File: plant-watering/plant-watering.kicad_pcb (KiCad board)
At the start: 2 copper layers, 11 parts, among them J1 Conn_01x03_Male, J2 Conn_01x03_Male, J3 Conn_01x03_Male, J4 Screw_Terminal_01x02, Q1 BC337, Q2 BC337, Q3 BC337, U1 ESP32-DEVKITC-32D

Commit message: added many schematicy
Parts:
- added J5: Screw_Terminal_01x02, Terminal_Blocks:TerminalBlock_bornier-2_P5.08mm, F.Cu at (142.2, 89.4)
- added J6: Screw_Terminal_01x02, Terminal_Blocks:TerminalBlock_bornier-2_P5.08mm, F.Cu at (142.2, 98.5)
- added J7: Screw_Terminal_01x02, Terminal_Blocks:TerminalBlock_bornier-2_P5.08mm, F.Cu at (153.8, 89.4)
- added K1: HJR-4102-L-05V, HJR-4102-L-05V:RELAY_HJR-4102-L-05V, F.Cu at (148.3, 62.5)
- added K2: HJR-4102-L-05V, HJR-4102-L-05V:RELAY_HJR-4102-L-05V, F.Cu at (148.3, 74.5)
- added K3: HJR-4102-L-05V, HJR-4102-L-05V:RELAY_HJR-4102-L-05V, F.Cu at (166.2, 62.5)
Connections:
- J3 pad 3: GPIO33 -> GPIO32
- U1 pad 5: Net-(U1-Pad5) -> GPIO34
- U1 pad 7: Net-(U1-Pad7) -> GPIO32
- U1 pad 8: Net-(U1-Pad8) -> GPIO33

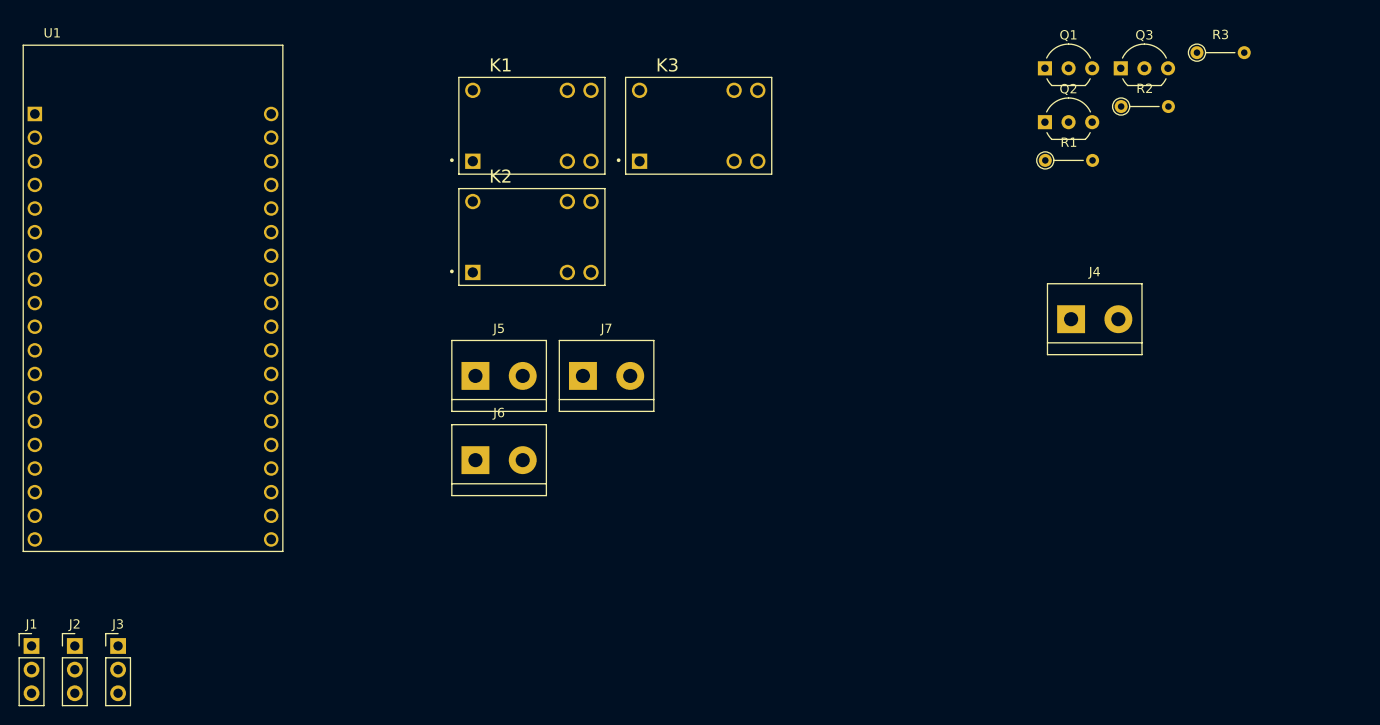
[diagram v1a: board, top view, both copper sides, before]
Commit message: edited schematic & started pcb design
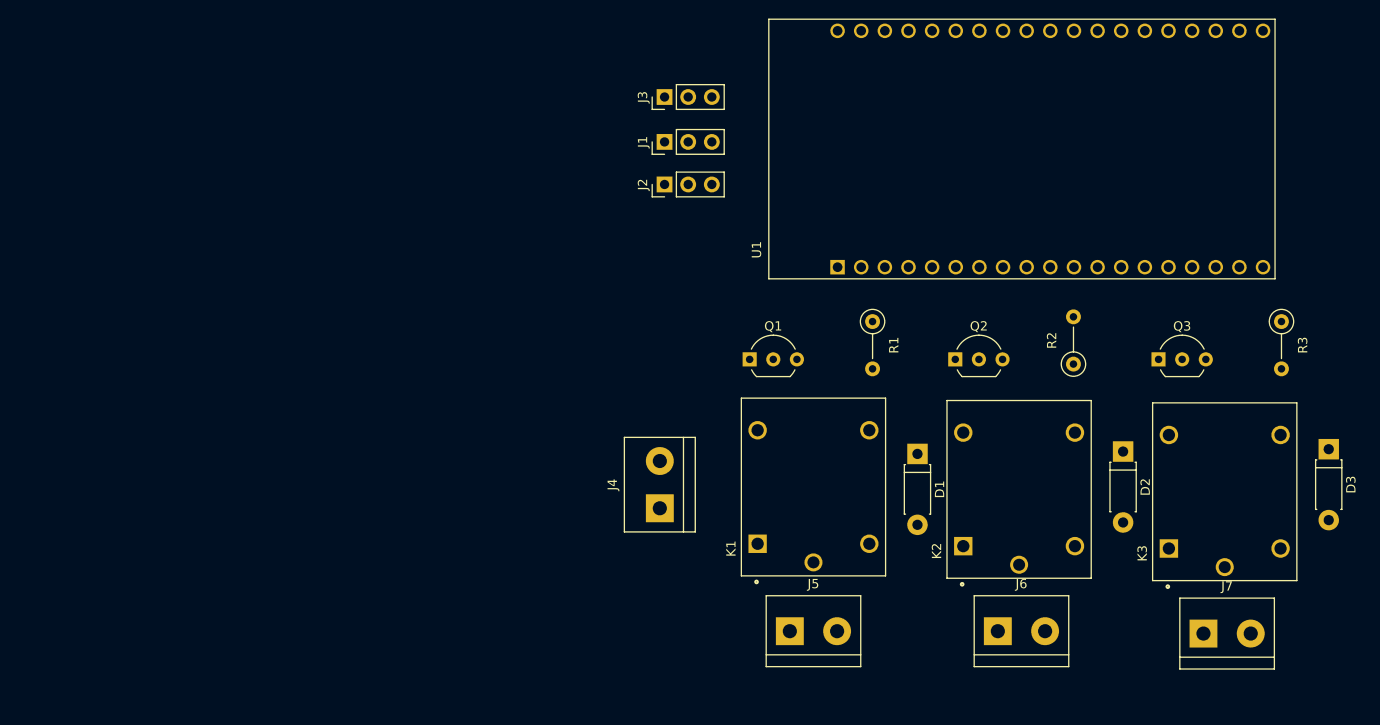
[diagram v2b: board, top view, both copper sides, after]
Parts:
- added D1: D, Diodes_ThroughHole:D_DO-41_SOD81_P7.62mm_Horizontal, F.Cu at (189.7, 97.8)
- added D2: D, Diodes_ThroughHole:D_DO-41_SOD81_P7.62mm_Horizontal, F.Cu at (211.8, 97.5)
- added D3: D, Diodes_ThroughHole:D_DO-41_SOD81_P7.62mm_Horizontal, F.Cu at (233.9, 97.3)
- J4: value Screw_Terminal_01x02 -> Input
- J5: value Screw_Terminal_01x02 -> M1
- J6: value Screw_Terminal_01x02 -> M2
- J7: value Screw_Terminal_01x02 -> M3
- K1, K2, K3: value HJR-4102-L-05V -> SRD-05VDC-SL-C; footprint HJR-4102-L-05V:RELAY_HJR-4102-L-05V -> SRD-05VDC-SL-C:RELAY_SRD-05VDC-SL-C
- R1, R2, R3: footprint Resistors:R_Axial_DIN0204_L3.6mm_D1.6mm_P5.08mm_Vertical -> Resistors_ThroughHole:R_Axial_DIN0207_L6.3mm_D2.5mm_P5.08mm_Vertical
- moved U1 94.7 mm to (200.9, 65.0), turned to 90 degrees
- moved J1 87.0 mm to (162.6, 64.3), turned to 90 degrees
- moved J3 83.2 mm to (162.6, 59.4), turned to 90 degrees
- moved J2 80.5 mm to (162.6, 68.8), turned to 90 degrees
- moved J7 72.2 mm to (220.5, 117.1)
- moved K3 68.9 mm to (222.8, 101.9), turned to 90 degrees
- moved J6 59.1 mm to (198.4, 116.8)
- moved K2 59.0 mm to (200.7, 101.6), turned to 90 degrees
- moved K1 49.2 mm to (178.6, 101.3), turned to 90 degrees
- moved J4 48.6 mm to (162.1, 103.6), turned to 90 degrees
- moved Q1 44.6 mm to (171.7, 87.6)
- moved J5 43.5 mm to (176.0, 116.8)
- moved Q3 31.5 mm to (215.6, 87.6)
- moved R3 30.3 mm to (228.9, 83.6), turned to 270 degrees
- moved R2 28.1 mm to (206.5, 88.1), turned to 90 degrees
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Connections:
- J4 pad 1: +5V -> GND
- J4 pad 2: GND -> +5V
- J5 pad 1: M1 -> GND
- J5 pad 2: GND -> M1
- J6 pad 1: M2 -> GND
- J6 pad 2: GND -> M2
- J7 pad 1: M3 -> GND
- J7 pad 2: GND -> M3
- Q1 pad 1: +5V -> RelayS1
- Q1 pad 3: RelayS1 -> GND
- Q2 pad 1: +5V -> RelayS2
- Q2 pad 3: RelayS2 -> GND
- Q3 pad 1: +5V -> RelayS3
- Q3 pad 3: RelayS3 -> GND

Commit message: started pcb design
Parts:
- added REF**: MountingHole_3.2mm_M3, MountingHole:MountingHole_3.2mm_M3, F.Cu at (234.5, 54.9)
- added REF**: MountingHole_3.2mm_M3, MountingHole:MountingHole_3.2mm_M3, F.Cu at (234.5, 116.8)
- added REF**: MountingHole_3.2mm_M3, MountingHole:MountingHole_3.2mm_M3, F.Cu at (161.5, 116.8)
- added REF**: MountingHole_3.2mm_M3, MountingHole:MountingHole_3.2mm_M3, F.Cu at (161.5, 54.9)
- moved J3 9.20 mm to (168.4, 52.3), turned to 0 degrees
- moved J2 7.12 mm to (168.4, 72.9), turned to 0 degrees
- moved J1 6.11 mm to (168.4, 62.5), turned to 0 degrees
- moved J4 5.57 mm to (164.3, 98.6), turned to 270 degrees
- moved R2 5.08 mm to (206.5, 83.1), turned to 270 degrees
- moved U1 0.51 mm to (200.9, 65.5)
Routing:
- added copper zone on B.Cu, net GND

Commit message: added several parts#
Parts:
- added D4: D, Diodes_ThroughHole:D_DO-41_SOD81_P7.62mm_Horizontal, F.Cu at (266.2, 80.8)
- added D5: D, Diodes_ThroughHole:D_DO-41_SOD81_P7.62mm_Horizontal, F.Cu at (266.2, 76.3)
- added D6: D, Diodes_ThroughHole:D_DO-41_SOD81_P7.62mm_Horizontal, F.Cu at (287.5, 59.3)
- added J10: Conn_01x03_Male, Pin_Headers:Pin_Header_Straight_1x03_Pitch2.54mm, F.Cu at (320.2, 76.9)
- added J11: M1, Terminal_Blocks:TerminalBlock_bornier-2_P5.08mm, F.Cu at (257.8, 99.7)
- added J12: M2, Terminal_Blocks:TerminalBlock_bornier-2_P5.08mm, F.Cu at (246.3, 108.8)
- added J13: M3, Terminal_Blocks:TerminalBlock_bornier-2_P5.08mm, F.Cu at (246.3, 99.7)
- added J14: Conn_01x04_Female, Pin_Headers:Pin_Header_Straight_1x04_Pitch2.54mm, F.Cu at (283.0, 97.5)
- added J8: Conn_01x03_Male, Pin_Headers:Pin_Header_Straight_1x03_Pitch2.54mm, F.Cu at (310.9, 76.9)
- added J9: Conn_01x03_Male, Pin_Headers:Pin_Header_Straight_1x03_Pitch2.54mm, F.Cu at (315.5, 76.9)
- added K4: SRD-05VDC-SL-C, SRD-05VDC-SL-C:RELAY_SRD-05VDC-SL-C, F.Cu at (275.3, 65.6)
- added K5: SRD-05VDC-SL-C, SRD-05VDC-SL-C:RELAY_SRD-05VDC-SL-C, F.Cu at (254.0, 82.6)
- added K6: SRD-05VDC-SL-C, SRD-05VDC-SL-C:RELAY_SRD-05VDC-SL-C, F.Cu at (254.0, 65.6)
- added Q4: BC337, TO_SOT_Packages_THT:TO-92_Inline_Wide, F.Cu at (327.1, 64.6)
- added Q5: BC337, TO_SOT_Packages_THT:TO-92_Inline_Wide, F.Cu at (318.9, 64.6)
- added Q6: BC337, TO_SOT_Packages_THT:TO-92_Inline_Wide, F.Cu at (310.1, 68.8)
- added R4: 5k, Resistors_ThroughHole:R_Axial_DIN0207_L6.3mm_D2.5mm_P5.08mm_Vertical, F.Cu at (319.5, 59.2)
- added R5: 5k, Resistors_ThroughHole:R_Axial_DIN0207_L6.3mm_D2.5mm_P5.08mm_Vertical, F.Cu at (310.7, 63.4)
- added R6: 5k, Resistors_ThroughHole:R_Axial_DIN0207_L6.3mm_D2.5mm_P5.08mm_Vertical, F.Cu at (310.7, 59.2)
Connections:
- R2 pad 1: GPIO14 -> GPIO13
- R3 pad 1: GPIO27 -> GPIO17
- U1 pad 12: GPIO14 -> Net-(U1-Pad12)
- U1 pad 15: Net-(U1-Pad15) -> GPIO13
- U1 pad 22: Net-(U1-Pad22) -> GPIO22
- U1 pad 25: Net-(U1-Pad25) -> GPIO21
- U1 pad 30: Net-(U1-Pad30) -> GPIO17
- U1 pad 31: Net-(U1-Pad31) -> GPIO16
- U1 pad 6: Net-(U1-Pad6) -> GPIO35

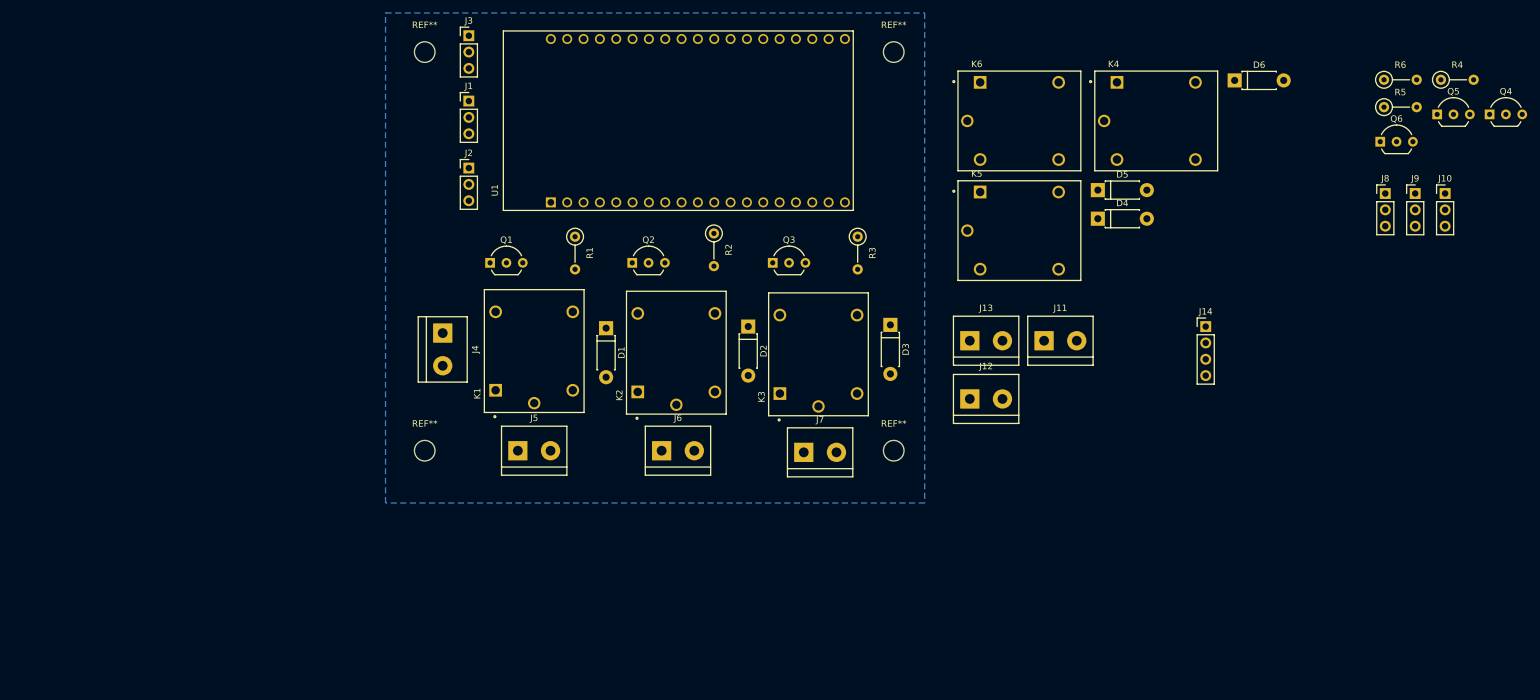
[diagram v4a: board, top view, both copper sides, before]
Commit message: changed pcb parts
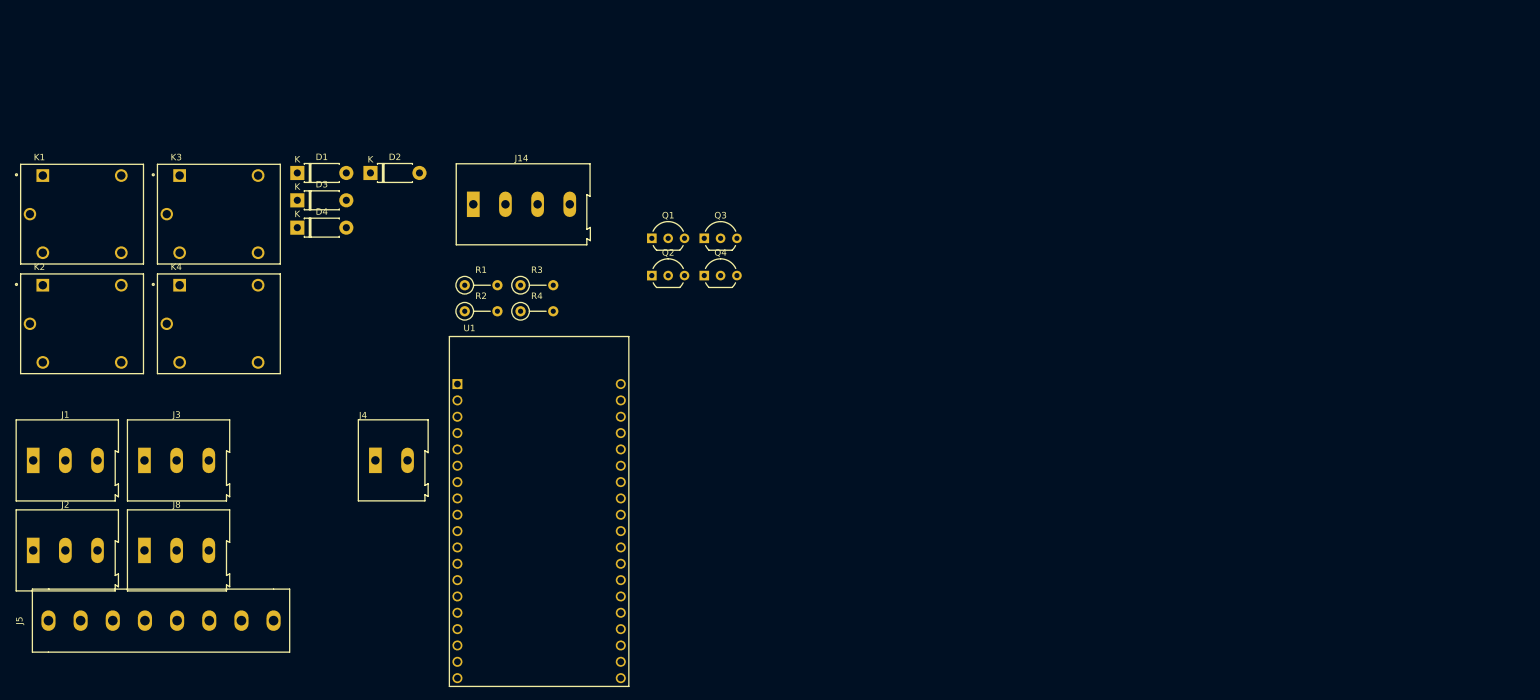
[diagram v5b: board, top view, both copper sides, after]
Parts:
- removed D5, D6: D, Diodes_ThroughHole:D_DO-41_SOD81_P7.62mm_Horizontal
- removed J10, J9: Conn_01x03_Male, Pin_Headers:Pin_Header_Straight_1x03_Pitch2.54mm
- removed J11: M1, Terminal_Blocks:TerminalBlock_bornier-2_P5.08mm
- removed J12, J6: M2, Terminal_Blocks:TerminalBlock_bornier-2_P5.08mm
- removed J13, J7: M3, Terminal_Blocks:TerminalBlock_bornier-2_P5.08mm
- removed K5, K6: SRD-05VDC-SL-C, SRD-05VDC-SL-C:RELAY_SRD-05VDC-SL-C
- removed Q5, Q6: BC337, TO_SOT_Packages_THT:TO-92_Inline_Wide
- removed R5, R6: 5k, Resistors_ThroughHole:R_Axial_DIN0207_L6.3mm_D2.5mm_P5.08mm_Vertical
- removed REF** (x4): MountingHole_3.2mm_M3, MountingHole:MountingHole_3.2mm_M3
- D1, D2, D3, D4: footprint Diodes_ThroughHole:D_DO-41_SOD81_P7.62mm_Horizontal -> Diode_THT:D_DO-41_SOD81_P7.62mm_Horizontal
- J1, J2, J3, J8: footprint Pin_Headers:Pin_Header_Straight_1x03_Pitch2.54mm -> TerminalBlock:TerminalBlock_Altech_AK300-3_P5.00mm
- J14: footprint Pin_Headers:Pin_Header_Straight_1x04_Pitch2.54mm -> TerminalBlock:TerminalBlock_Altech_AK300-4_P5.00mm
- J4: footprint Terminal_Blocks:TerminalBlock_bornier-2_P5.08mm -> TerminalBlock:TerminalBlock_Altech_AK300-2_P5.00mm
- J5: value M1 -> Screw_Terminal_01x08; footprint Terminal_Blocks:TerminalBlock_bornier-2_P5.08mm -> TerminalBlock:ScrewTerminal_1x8_P5.00
- Q1, Q2, Q3, Q4: footprint TO_SOT_Packages_THT:TO-92_Inline_Wide -> Package_TO_SOT_THT:TO-92_Inline_Wide
- R1, R2, R3, R4: footprint Resistors_ThroughHole:R_Axial_DIN0207_L6.3mm_D2.5mm_P5.08mm_Vertical -> Resistor_THT:R_Axial_DIN0207_L6.3mm_D2.5mm_P5.08mm_Vertical
- moved J8 200.7 mm to (118.0, 132.3)
- moved K4 149.1 mm to (129.5, 97.1)
- moved R4 147.5 mm to (176.4, 95.2)
- moved Q4 124.6 mm to (205.0, 89.6)
- moved D4 124.5 mm to (141.7, 82.2)
- moved J14 115.4 mm to (169.1, 78.5)
- moved K3 95.7 mm to (129.5, 80.1), turned to 0 degrees
- moved D3 94.2 mm to (141.7, 77.9), turned to 0 degrees
- moved K2 92.5 mm to (108.3, 97.1), turned to 0 degrees
- moved J2 90.1 mm to (100.7, 132.3)
- moved J1 87.8 mm to (100.7, 118.3)
- moved J3 83.1 mm to (118.0, 118.3)
- moved J5 82.3 mm to (98.0, 143.3), turned to 90 degrees
- moved K1 73.4 mm to (108.3, 80.1), turned to 0 degrees
- moved U1 64.4 mm to (179.3, 126.2), turned to 0 degrees
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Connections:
- J5 pad 1: GND -> M1
- J5 pad 2: M1 -> GND
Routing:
- removed copper zone on B.Cu, net GND

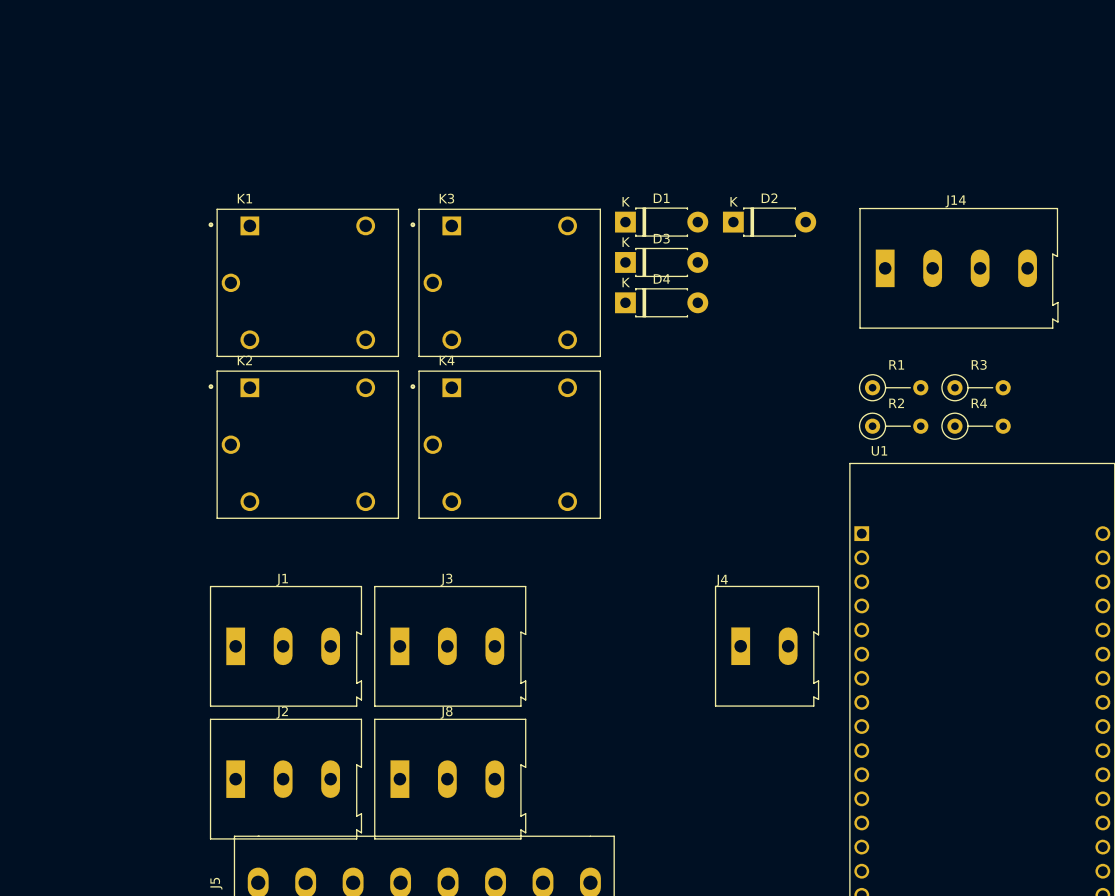
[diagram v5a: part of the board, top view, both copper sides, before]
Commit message: changed parts on pcb
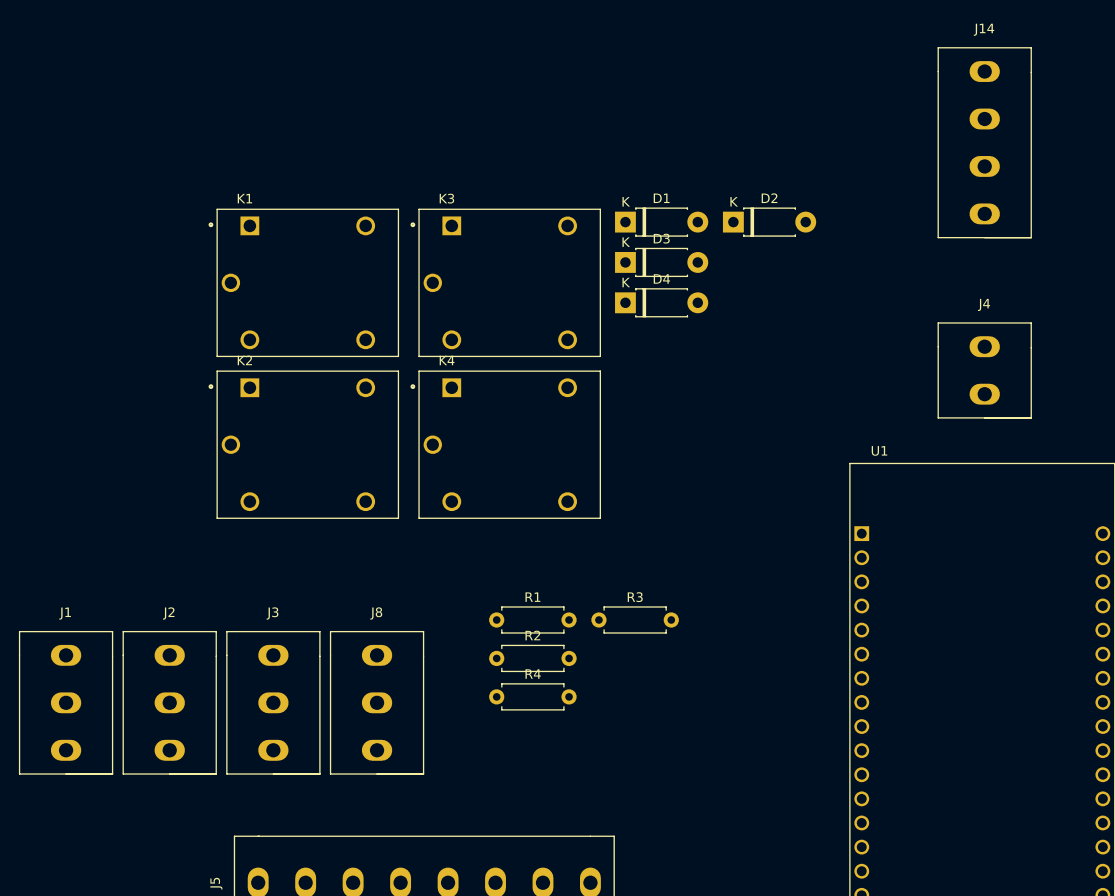
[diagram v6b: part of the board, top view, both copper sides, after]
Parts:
- J1, J2, J3, J8: footprint TerminalBlock:TerminalBlock_Altech_AK300-3_P5.00mm -> TerminalBlock:ScrewTerminal_1x3_P5.00
- J14: footprint TerminalBlock:TerminalBlock_Altech_AK300-4_P5.00mm -> TerminalBlock:ScrewTerminal_1x4_P5.00
- J4: footprint TerminalBlock:TerminalBlock_Altech_AK300-2_P5.00mm -> TerminalBlock:ScrewTerminal_1x2_P5.00
- R1, R2, R3, R4: footprint Resistor_THT:R_Axial_DIN0207_L6.3mm_D2.5mm_P5.08mm_Vertical -> Resistor_THT:R_Axial_DIN0207_L6.3mm_D2.5mm_P7.62mm_Horizontal
- moved R4 56.1 mm to (128.2, 123.7)
- moved R1 46.5 mm to (128.2, 115.6)
- moved R2 46.5 mm to (128.2, 119.6)
- moved R3 44.8 mm to (138.9, 115.6)
- moved J4 44.7 mm to (179.6, 81.8)
- moved J14 27.8 mm to (179.6, 52.8)
- moved J2 19.3 mm to (93.7, 114.3)
- moved J1 18.3 mm to (82.8, 114.3)
- moved J8 18.2 mm to (115.6, 114.3)
- moved J3 13.9 mm to (104.6, 114.3)
